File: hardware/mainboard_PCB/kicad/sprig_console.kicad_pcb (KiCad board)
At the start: 2 copper layers, 139.7 x 64.8 mm, 42 parts, among them J1 1020_battery_holder, J2 Conn_PinHeader_2x03_P2.54mm_V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, SW1 W, SW2 A, SW3 S, SW4 D, SW5 I, SW6 J, SW7 K, SW8 L, SW9 Slideswitch, U2 MAX98357AETE+, U5 Pico

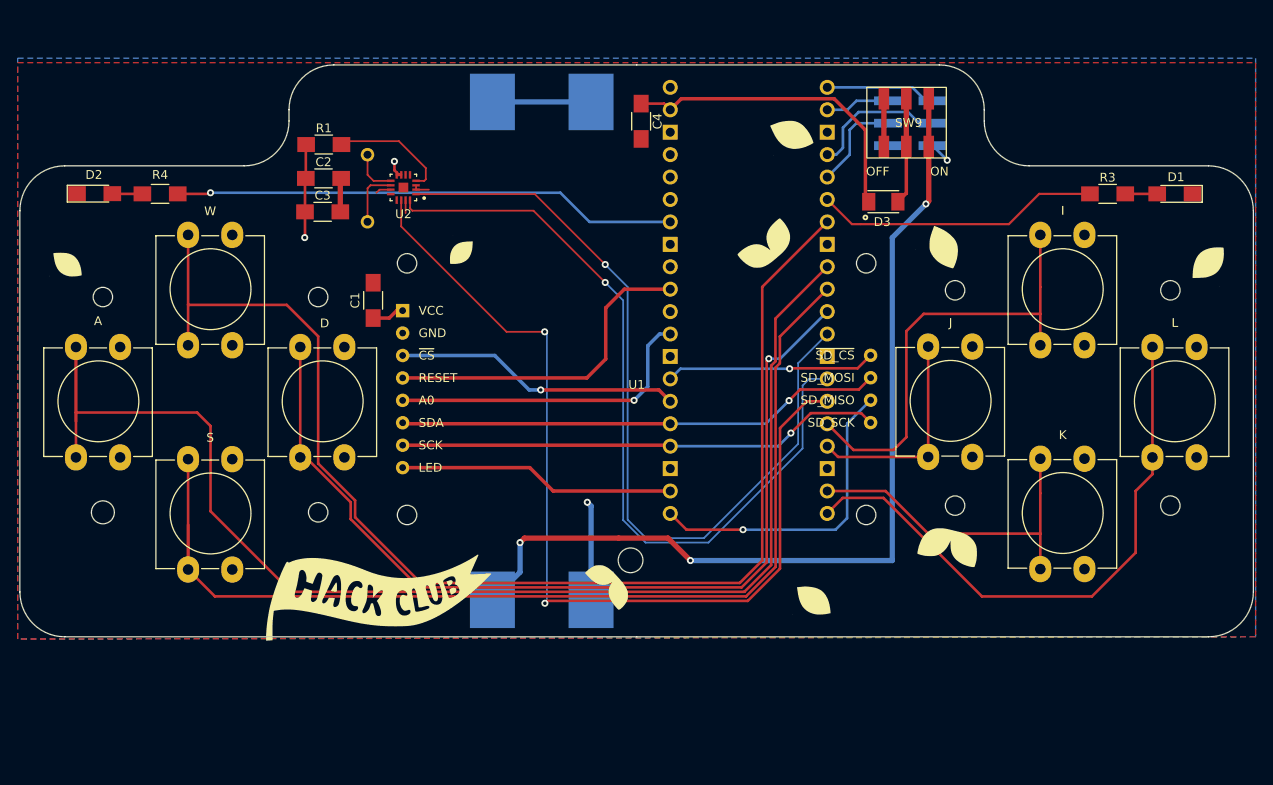
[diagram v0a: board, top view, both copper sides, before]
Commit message: resdesign of KiCad board file to a fully through hole version
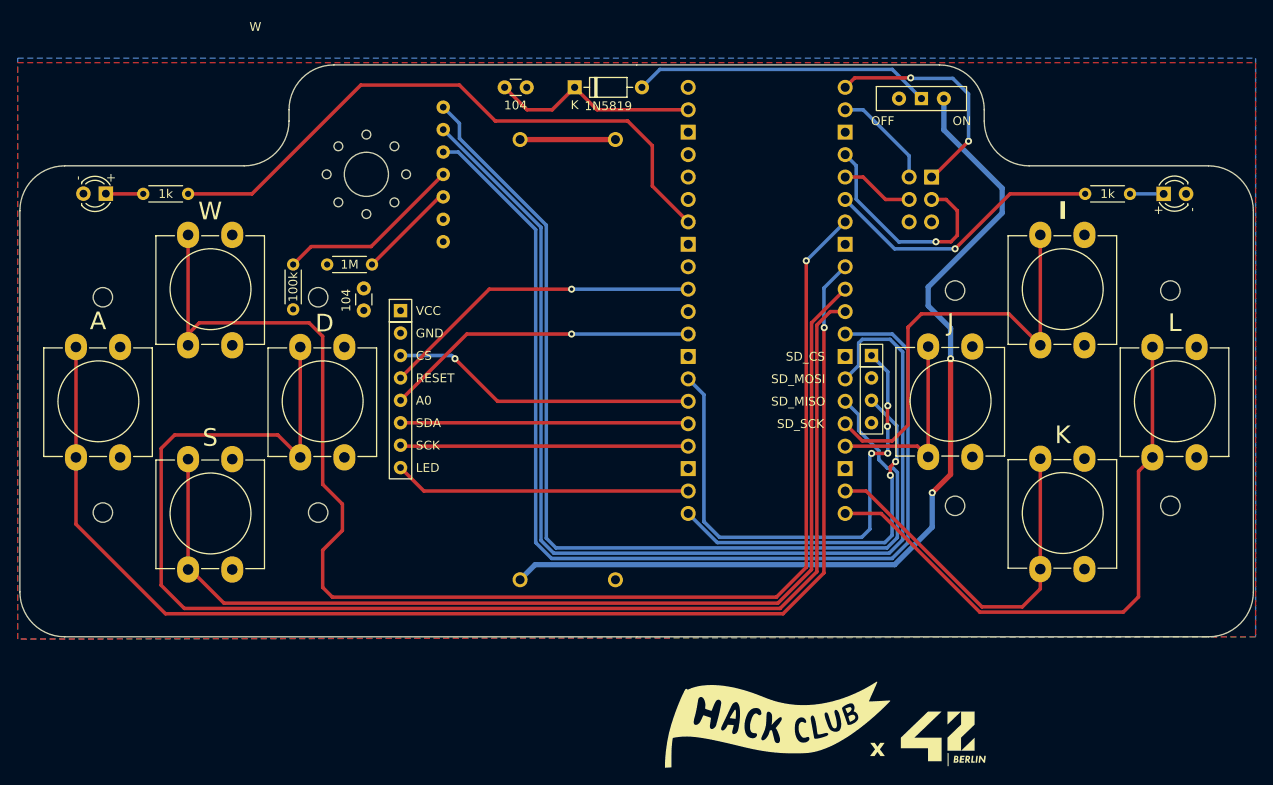
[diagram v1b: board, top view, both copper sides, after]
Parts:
- removed the ? at (212.9, 85.2)
- removed the ? at (91.9, 110.4)
- removed the ? at (116.3, 86.0)
- removed the ? at (188.5, 109.6)
- removed the ? at (91.9, 86.0)
- removed the ? at (116.3, 110.4)
- removed the ? at (212.9, 109.6)
- removed the ? at (188.5, 85.2)
- removed C2: 10uF, fab:C_1206
- removed C3: 0.1uF, fab:C_1206
- removed the G*** at (152.4, 94.0)
- removed the G*** at (202.0, 121.9)
- removed the G*** at (152.9, 91.9)
- removed the G*** at (100.0, 121.4)
- removed Ref**: Val**, footprints:usb
- added ?: , , F.Cu at (212.9, 109.6)
- added ?: , , F.Cu at (91.9, 110.4)
- added ?: , , F.Cu at (188.5, 109.6)
- added ?: , , F.Cu at (116.3, 110.4)
- added ?: , , F.Cu at (188.5, 85.2)
- added ?: , , F.Cu at (212.9, 85.2)
- added ?: , , F.Cu at (91.9, 86.0)
- added ?: , , F.Cu at (116.3, 86.0)
- added R2: 100k, Resistor_THT:R_Axial_DIN0204_L3.6mm_D1.6mm_P5.08mm_Horizontal, F.Cu at (113.5, 87.4)
- C1, C4: footprint fab:C_1206 -> Capacitor_THT:C_Disc_D3.0mm_W1.6mm_P2.50mm
- D1, D2: footprint fab:LED_1206 -> PCM_4ms_LED:LED_3mm_C1A2_Polarity_Indicator
- D3: value SD1206T020S1R0 -> 1N5819; footprint fab:Diode_Schotky_100V_1A_Mini_SMA -> Diode_THT:D_DO-35_SOD27_P7.62mm_Horizontal
- J1: value 1020_battery_holder -> 2 x AAA Battery Holder
- J2: footprint fab:PinHeader_2x03_P2.54mm_Vertical_SMD -> Connector_PinHeader_2.54mm:PinHeader_2x03_P2.54mm_Vertical
- LS1: footprint fab:CVS-1508 -> Library:1W_8Ohm_Speaker
- R1, R3, R4: footprint fab:R_1206 -> Resistor_THT:R_Axial_DIN0204_L3.6mm_D1.6mm_P5.08mm_Horizontal
- SW9: footprint slideSWSMD:slideswitchCK -> Button_Switch_THT:SW_Slide-03_Wuerth-WS-SLTV_10x2.5x6.4_P2.54mm
- U1: value ~ -> Adafruit_TFT_ST7735; footprint sprig:TFT_MSP1803 -> Library:Generic_1.8Inch_TFT_120x160
- U2: footprint local:QFN50P300X300X80-17N -> Library:Max98357A_ClassD_I2S_Mono_Amp_BreakoutBoard; moved to B.Cu
- U5: value Pico -> RPi Pico
- moved G*** 70.8 mm to (119.9, 135.4)
- moved G*** 47.4 mm to (168.4, 134.4)
- moved D3 37.3 mm to (145.4, 62.2)
- moved G*** 27.7 mm to (89.3, 121.4)
- moved G*** 16.3 mm to (215.1, 137.9)
- moved C4 15.9 mm to (137.5, 62.2), turned to 0 degrees
- moved R1 13.6 mm to (117.3, 82.3)
- moved J2 6.56 mm to (185.8, 72.4)
- moved SW9 6.31 mm to (184.7, 63.5)
- moved R4 3.17 mm to (101.6, 74.3)
- moved U2 3.12 mm to (123.2, 72.1), turned to -90 degrees
- moved R3 2.54 mm to (203.2, 74.3)
- moved U5 2.03 mm to (167.1, 86.4)
- moved LS1 1.58 mm to (121.8, 72.1)
- moved J1 1.58 mm to (144.6, 93.1)
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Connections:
- R1 pad 2: Net-(U2-~{SD_MODE}) -> Net-(U2-SD)
- U1 pad 1: +3V3 -> LITE
- U1 pad 10: MOSI -> GND
- U1 pad 11: MISO -> unconnected-(U1-SD_MOSI-Pad11)
- U1 pad 12: SCK -> unconnected-(U1-SD_SDK-Pad12)
- U1 pad 2: GND -> MISO
- U1 pad 3: TFT_CS -> SCK
- U1 pad 4: RESET -> MOSI
- U1 pad 5: D/C -> TFT_CS
- U1 pad 6: MOSI -> CARD_CS
- U1 pad 7: SCK -> D/C
- U1 pad 8: LITE -> RESET
- U1 pad 9: CARD_CS -> +3V3
- U2 pad 1: DIN -> LRCLK
- U2 pad 2: GND -> BCLK
- U2 pad 3: GND -> DIN
- U2 pad 4: Net-(U2-~{SD_MODE}) -> Net-(U2-GAIN)
- U2 pad 5: (no net) -> Net-(U2-SD)
- U2 pad 6: (no net) -> GND
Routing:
- net BTN_D: track 107.2 -> 154.3 mm, vias 1 -> 0
- net CARD_CS: track 23.8 -> 59.2 mm, vias 1 -> 4
- net BCLK: track 90.3 -> 125.0 mm, vias 1 -> 0
- net DIN: track 93.1 -> 122.9 mm, vias 1 -> 0
- net GND: track 23.2 -> 0.00 mm, vias 2 -> 0
- net MOSI: track 55.6 -> 32.6 mm, vias 1 -> 0
- net SCK: track 55.3 -> 32.6 mm, vias 1 -> 0
- net Net-(D3-A): track 12.4 -> 33.9 mm
- net Net-(U2-GAIN): track 0.00 -> 21.2 mm
- net +3V3: track 15.9 -> 0.00 mm, vias 2 -> 0
- net BTN_W: track 142.6 -> 158.0 mm, vias 0 -> 1
- net GPIO0: track 11.8 -> 26.4 mm, vias 0 -> 2
- net Net-(U2-~{SD_MODE}): track 13.9 -> 0.00 mm
- net LED_L: track 57.2 -> 70.8 mm, vias 1 -> 0
- net Net-(D3-K): track 36.9 -> 23.9 mm
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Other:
- board text added: "A LOW-COST THROUGH-HOLE VERSION OF THE HACK CLUB SPRIG - https://github.com/fablabnk/trigg"
- board text added: "W"
- board text added: "x"

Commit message: board ready for v1.0 production at jlcpcb
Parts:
- moved G*** 61.1 mm to (137.4, 76.8)
- moved R1 37.6 mm to (129.5, 117.9), turned to 180 degrees
- moved R2 32.2 mm to (129.5, 115.3), turned to 180 degrees
- moved C1 29.7 mm to (131.8, 115.3), turned to -90 degrees
- moved G*** 23.9 mm to (149.6, 119.6)
- turned D1 to 0 degrees
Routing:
- net Net-(U2-SD): track 11.2 -> 53.4 mm
- net Net-(U2-GAIN): track 21.2 -> 53.3 mm
- net Net-(D1-A): track 3.81 -> 7.72 mm
- net BTN_D: track 154.3 -> 155.8 mm
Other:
- board text added: "A LOW-COST THROUGH-HOLE VERSION OF THE HACK CLUB SPRIG :"
- board text added: "JLCJLCJLCJLC"
- board text added: "V1.0"
- board text added: "https://github.com/fablabnk/trigg"
- board text removed: "A LOW-COST THROUGH-HOLE VERSION OF THE HACK CLUB SPRIG - https://github.com/fablabnk/trigg"
- board text removed: "W"
